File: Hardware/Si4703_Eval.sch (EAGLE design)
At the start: 37 parts, among them U1 SI4703, U3 TPA6111, Y1 32.768kHz

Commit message: fixing I2C breakout order, adding board name to file
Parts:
- added U$1: REVISION, SparkFun-Aesthetics:REVISION
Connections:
- net 3.3V: now also JP1.7; no longer JP1.8
- net GND: now also JP1.8; no longer JP1.7
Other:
- note added: "Toni Klopfenstein"
- note removed: "All 0603 footprints"
- note removed: "Changed to SMD audio connector"
- note removed: "Changed to current OSHW logo"
- note removed: "Changes to v1.2 (4/27/11)"
- note removed: "Changes to v1.3 (12/13/13)"
- note removed: "Removed via under IC to improve reflow."
- note removed: "Updated Si4703 footprint"

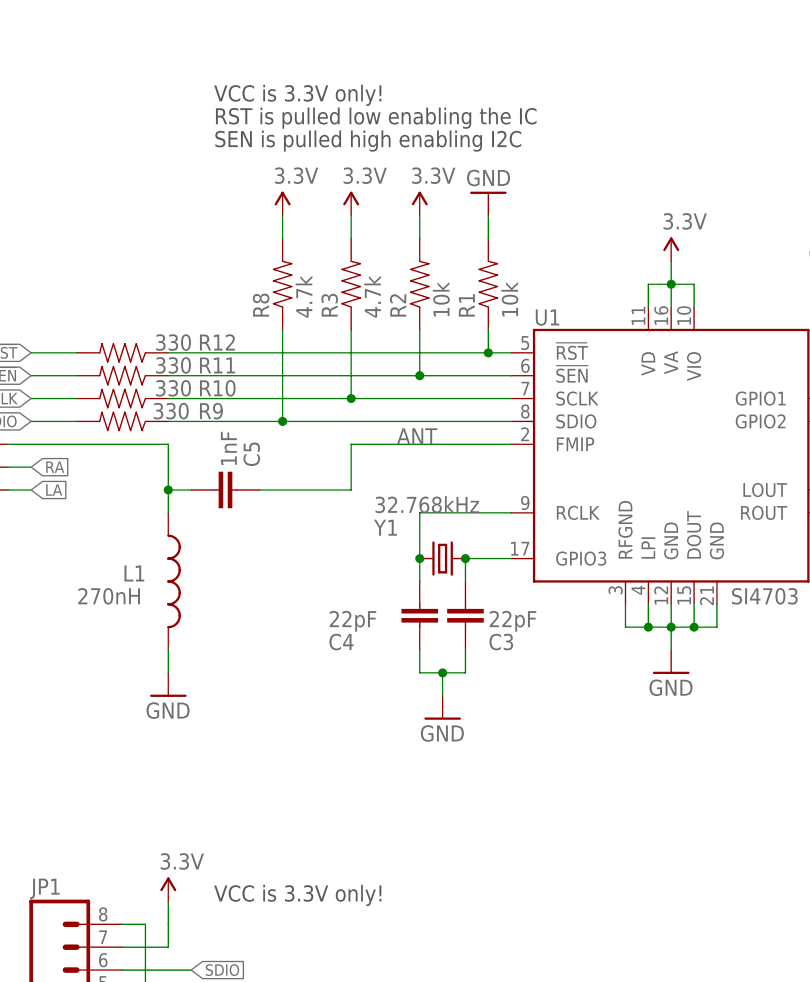
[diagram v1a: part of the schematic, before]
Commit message: Fixing review complaints on version number and upside down ground on schematic
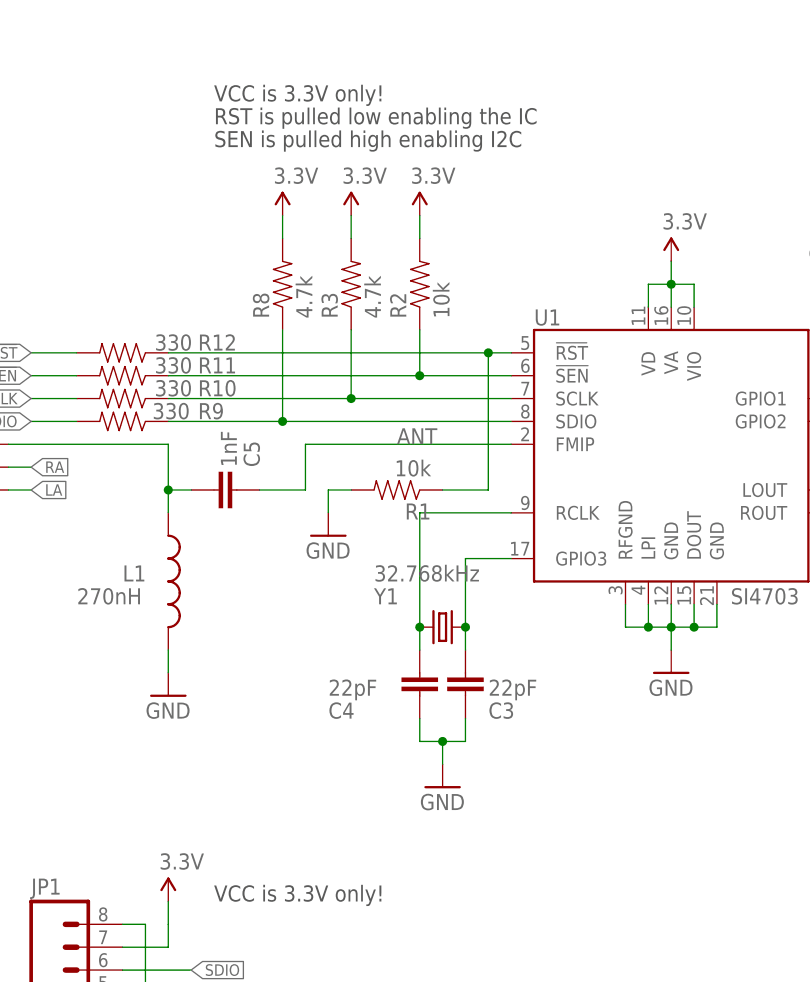
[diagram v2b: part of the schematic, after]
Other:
- moved on the sheet: C3, C4, R1, Y1
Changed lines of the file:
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@@
 <attribute name="VALUE" x="108.204" y="93.98" size="1.778" layer="96"/>
 </instance>
-<instance part="Y1" gate="G$1" x="76.2" y="99.06" smashed="yes" rot="R180">
-<attribute name="NAME" x="68.58" y="101.6" size="1.778" layer="95"/>
-<attribute name="VALUE" x="68.58" y="104.14" size="1.778" layer="96"/>
+<instance part="Y1" gate="G$1" x="76.2" y="91.44" smashed="yes" rot="R180">
+<attribute name="NAME" x="68.58" y="93.98" size="1.778" layer="95"/>
+<attribute name="VALUE" x="68.58" y="96.52" size="1.778" layer="96"/>
 </instance>
 <instance part="C1" gate="G$1" x="119.38" y="142.24"/>
 <instance part="C2" gate="G$1" x="132.08" y="142.24"/>
 <instance part="GND1" gate="1" x="101.6" y="86.36"/>
-<instance part="C3" gate="G$1" x="78.74" y="93.98" smashed="yes" rot="R180">
-<attribute name="NAME" x="81.28" y="88.9" size="1.778" layer="95"/>
-<attribute name="VALUE" x="81.28" y="91.44" size="1.778" layer="96"/>
-</instance>
-<instance part="C4" gate="G$1" x="73.66" y="93.98" smashed="yes" rot="R180">
-<attribute name="NAME" x="63.5" y="88.9" size="1.778" layer="95"/>
-<attribute name="VALUE" x="63.5" y="91.44" size="1.778" layer="96"/>
-</instance>
-<instance part="GND2" gate="1" x="76.2" y="81.28"/>
+<instance part="C3" gate="G$1" x="78.74" y="86.36" smashed="yes" rot="R180">
+<attribute name="NAME" x="81.28" y="81.28" size="1.778" layer="95"/>
+<attribute name="VALUE" x="81.28" y="83.82" size="1.778" layer="96"/>
+</instance>
+<instance part="C4" gate="G$1" x="73.66" y="86.36" smashed="yes" rot="R180">
+<attribute name="NAME" x="63.5" y="81.28" size="1.778" layer="95"/>
+<attribute name="VALUE" x="63.5" y="83.82" size="1.778" layer="96"/>
+</instance>
+<instance part="GND2" gate="1" x="76.2" y="73.66"/>
 <instance part="C5" gate="G$1" x="50.8" y="106.68" smashed="yes" rot="R270">
 <attribute name="NAME" x="55.88" y="109.22" size="1.778" layer="95" rot="R90"/>
@@
 </instance>
 <instance part="GND3" gate="1" x="45.72" y="83.82"/>
-<instance part="R1" gate="G$1" x="81.28" y="129.54" rot="R90"/>
+<instance part="R1" gate="G$1" x="71.12" y="106.68" rot="R180"/>
 <instance part="R2" gate="G$1" x="73.66" y="129.54" rot="R90"/>
 <instance part="R3" gate="G$1" x="66.04" y="129.54" rot="R90"/>
@@
 <attribute name="VALUE" x="44.196" y="122.174" size="1.778" layer="96"/>
 </instance>
-<instance part="GND4" gate="1" x="81.28" y="139.7" rot="R180"/>
+<instance part="GND4" gate="1" x="63.5" y="101.6"/>
 <instance part="JP1" gate="G$1" x="35.56" y="48.26"/>
 <instance part="GND10" gate="1" x="43.18" y="33.02"/>
@@
 </segment>
 <segment>
-<wire x1="78.74" y1="86.36" x2="78.74" y2="88.9" width="0.1524" layer="91"/>
-<wire x1="73.66" y1="88.9" x2="73.66" y2="86.36" width="0.1524" layer="91"/>
-<wire x1="73.66" y1="86.36" x2="76.2" y2="86.36" width="0.1524" layer="91"/>
-<wire x1="76.2" y1="86.36" x2="78.74" y2="86.36" width="0.1524" layer="91"/>
-<wire x1="76.2" y1="83.82" x2="76.2" y2="86.36" width="0.1524" layer="91"/>
-<junction x="76.2" y="86.36"/>
+<wire x1="78.74" y1="78.74" x2="78.74" y2="81.28" width="0.1524" layer="91"/>
+<wire x1="73.66" y1="81.28" x2="73.66" y2="78.74" width="0.1524" layer="91"/>
+<wire x1="73.66" y1="78.74" x2="76.2" y2="78.74" width="0.1524" layer="91"/>
+<wire x1="76.2" y1="78.74" x2="78.74" y2="78.74" width="0.1524" layer="91"/>
+<wire x1="76.2" y1="76.2" x2="76.2" y2="78.74" width="0.1524" layer="91"/>
+<junction x="76.2" y="78.74"/>
 <pinref part="C3" gate="G$1" pin="1"/>
 <pinref part="C4" gate="G$1" pin="1"/>
@@
 </segment>
 <segment>
-<wire x1="81.28" y1="137.16" x2="81.28" y2="134.62" width="0.1524" layer="91"/>
+<wire x1="63.5" y1="104.14" x2="63.5" y2="106.68" width="0.1524" layer="91"/>
+<wire x1="63.5" y1="106.68" x2="66.04" y2="106.68" width="0.1524" layer="91"/>
 <pinref part="R1" gate="G$1" pin="2"/>
 <pinref part="GND4" gate="1" pin="GND"/>
@@
 <net name="N$1" class="0">
 <segment>
-<wire x1="73.66" y1="99.06" x2="73.66" y2="96.52" width="0.1524" layer="91"/>
+<wire x1="73.66" y1="91.44" x2="73.66" y2="88.9" width="0.1524" layer="91"/>
 <wire x1="83.82" y1="104.14" x2="73.66" y2="104.14" width="0.1524" layer="91"/>
-<wire x1="73.66" y1="104.14" x2="73.66" y2="99.06" width="0.1524" layer="91"/>
-<junction x="73.66" y="99.06"/>
+<wire x1="73.66" y1="104.14" x2="73.66" y2="91.44" width="0.1524" layer="91"/>
+<junction x="73.66" y="91.44"/>
 <pinref part="Y1" gate="G$1" pin="2"/>
 <pinref part="C4" gate="G$1" pin="2"/>
@@
 <segment>
 <wire x1="83.82" y1="99.06" x2="78.74" y2="99.06" width="0.1524" layer="91"/>
-<wire x1="78.74" y1="99.06" x2="78.74" y2="96.52" width="0.1524" layer="91"/>
-<junction x="78.74" y="99.06"/>
+<wire x1="78.74" y1="99.06" x2="78.74" y2="91.44" width="0.1524" layer="91"/>
+<wire x1="78.74" y1="91.44" x2="78.74" y2="88.9" width="0.1524" layer="91"/>
+<junction x="78.74" y="91.44"/>
 <pinref part="U1" gate="G$1" pin="GPIO3"/>
 <pinref part="Y1" gate="G$1" pin="1"/>
@@
 <net name="ANT" class="0">
 <segment>
-<wire x1="55.88" y1="106.68" x2="66.04" y2="106.68" width="0.1524" layer="91"/>
-<wire x1="66.04" y1="106.68" x2="66.04" y2="111.76" width="0.1524" layer="91"/>
-<wire x1="66.04" y1="111.76" x2="83.82" y2="111.76" width="0.1524" layer="91"/>
+<wire x1="55.88" y1="106.68" x2="60.96" y2="106.68" width="0.1524" layer="91"/>
+<wire x1="60.96" y1="106.68" x2="60.96" y2="111.76" width="0.1524" layer="91"/>
+<wire x1="60.96" y1="111.76" x2="83.82" y2="111.76" width="0.1524" layer="91"/>
 <label x="71.12" y="111.76" size="1.778" layer="95"/>
 <pinref part="C5" gate="G$1" pin="1"/>
@@
 <segment>
 <wire x1="83.82" y1="121.92" x2="81.28" y2="121.92" width="0.1524" layer="91"/>
-<wire x1="81.28" y1="121.92" x2="81.28" y2="124.46" width="0.1524" layer="91"/>
+<wire x1="81.28" y1="121.92" x2="81.28" y2="106.68" width="0.1524" layer="91"/>
+<wire x1="81.28" y1="106.68" x2="76.2" y2="106.68" width="0.1524" layer="91"/>
 <wire x1="81.28" y1="121.92" x2="45.72" y2="121.92" width="0.1524" layer="91"/>
 <junction x="81.28" y="121.92"/>
